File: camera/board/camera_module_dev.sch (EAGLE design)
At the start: 57 parts, among them IC1 74541PW, IC2 74541PW, Q1 MOSFET-NCHANNELBSS123LT1G, Q2 MOSFET-NCHANNELBSS123LT1G

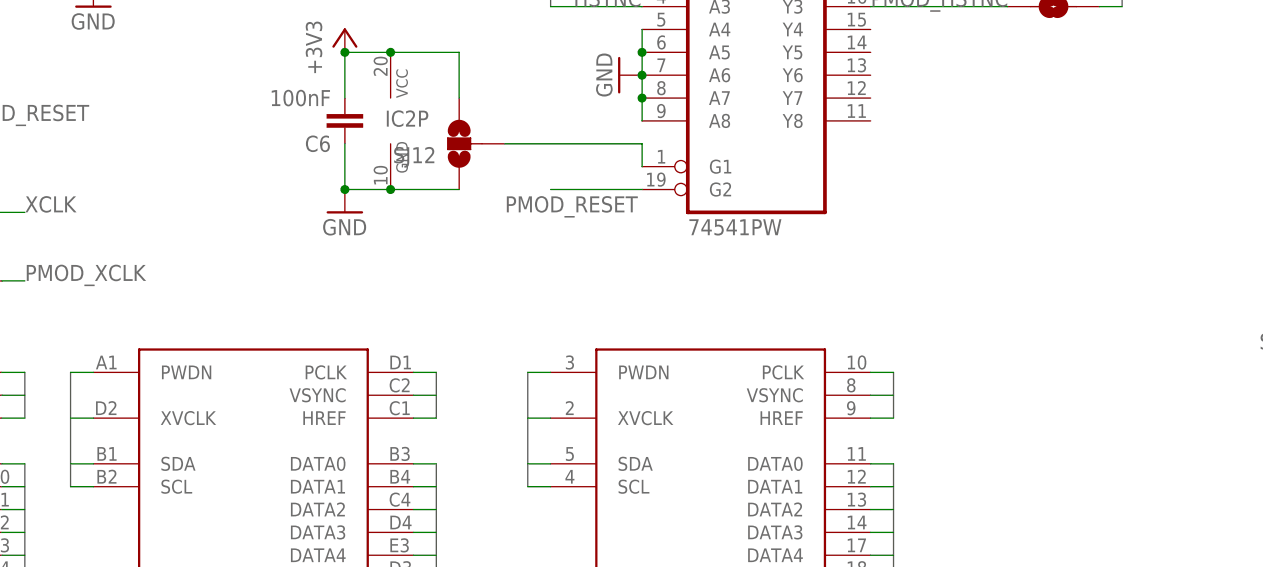
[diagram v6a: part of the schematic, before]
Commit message: Added note about camera voltages
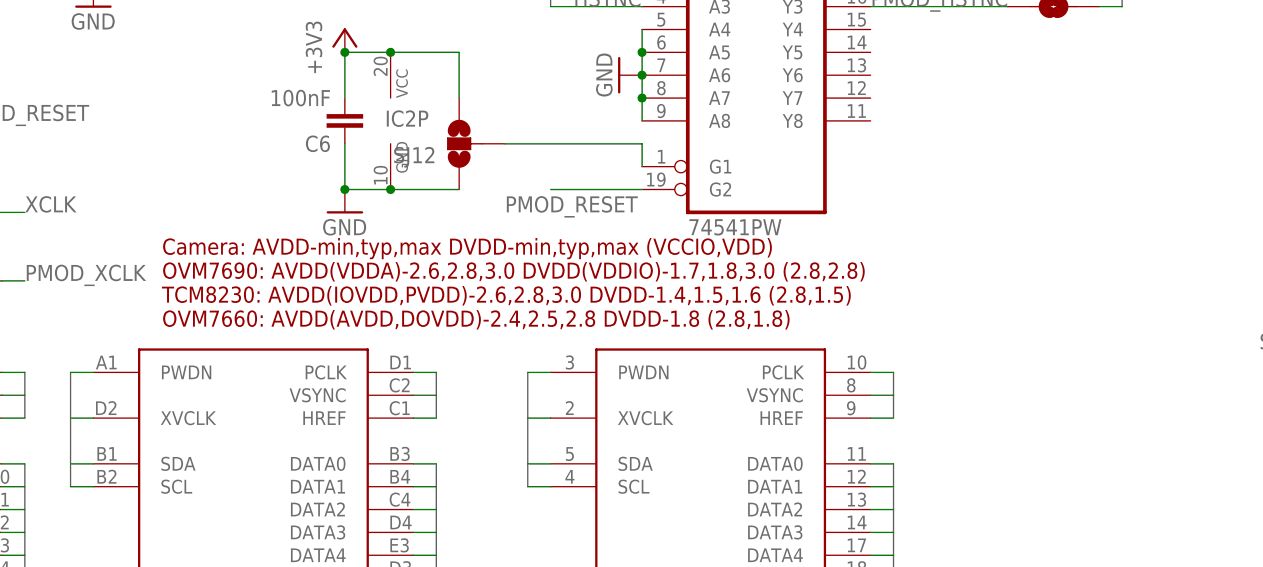
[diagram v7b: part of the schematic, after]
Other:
- note added: "Camera: AVDD-min,typ,max DVDD-min,typ,max (VCCIO,VDD) OVM7690: AVDD(VDDA)-2.6,2.8,3.0 DVDD(VDDIO)-1.7,1.8,3.0 (2.8,2.8) TCM8230: AVDD(IOVDD,PVDD)-2.6,2.8,3.0 DVDD-1.4,1.5,1.6 (2.8,1.5) OVM7660: AVDD(AVDD,DOVDD)-2.4,2.5,2.8 DVDD-1.8 (2.8,1.8)"
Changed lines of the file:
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@@
 <sheet>
 <plain>
+<text x="60.96" y="81.28" size="1.778" layer="94">Camera: AVDD-min,typ,max DVDD-min,typ,max (VCCIO,VDD)
+OVM7690: AVDD(VDDA)-2.6,2.8,3.0 DVDD(VDDIO)-1.7,1.8,3.0 (2.8,2.8)
+TCM8230: AVDD(IOVDD,PVDD)-2.6,2.8,3.0 DVDD-1.4,1.5,1.6 (2.8,1.5)
+OVM7660: AVDD(AVDD,DOVDD)-2.4,2.5,2.8 DVDD-1.8 (2.8,1.8)</text>
 </plain>
 <instances>
@@
 </schematic>
 </drawing>
+<compatibility>
+<note version="6.3" minversion="6.2.2" severity="warning">
+Since Version 6.2.2 text objects can contain more than one line,
+which will not be processed correctly with this version.
+</note>
+</compatibility>
 </eagle>

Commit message: Updated to r0.1. Fixed reset problems. Should be ready for shipping
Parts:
- removed SJ12, SJ13: (no value), SparkFun-Passives:SOLDERJUMPER_2WAYS
- U$7: REVISION r0.0 -> r0.1
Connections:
- removed net N$10: IC2A.G1, SJ12.2
- removed net N$7: IC1A.G1, SJ13.2
- net +3V3: no longer SJ12.3, SJ13.3
- net GND: now also IC1A.G1, IC1A.G2, IC2A.G1, IC2A.G2; no longer SJ12.1, SJ13.1
- net N$8: now also U$2G$1.PWDN
- net PMOD_RESET: no longer IC1A.G2, IC2A.G2, QG1.CON, U$1G$1.PWDN, U$2G$1.PWDN, U$3G$1.PWDN
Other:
- moved on the sheet: C6, IC1, IC2, IC2P
